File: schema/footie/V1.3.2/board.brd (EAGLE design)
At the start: 53 x 50.6 mm, 41 parts, among them T1 2N3565, U1 IRLML2246TRPBF, U2 USD-SOCKETNEW, U4 MCP73831, U5 3.3 regulator, U6 ATMEGA328P-AU

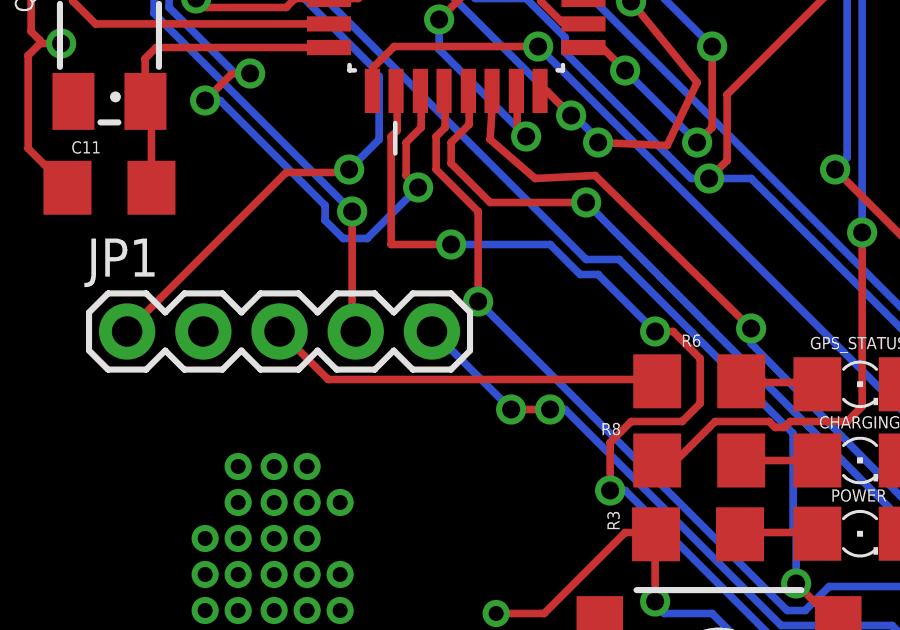
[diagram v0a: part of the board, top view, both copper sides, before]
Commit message: update parser fix schematic wiring
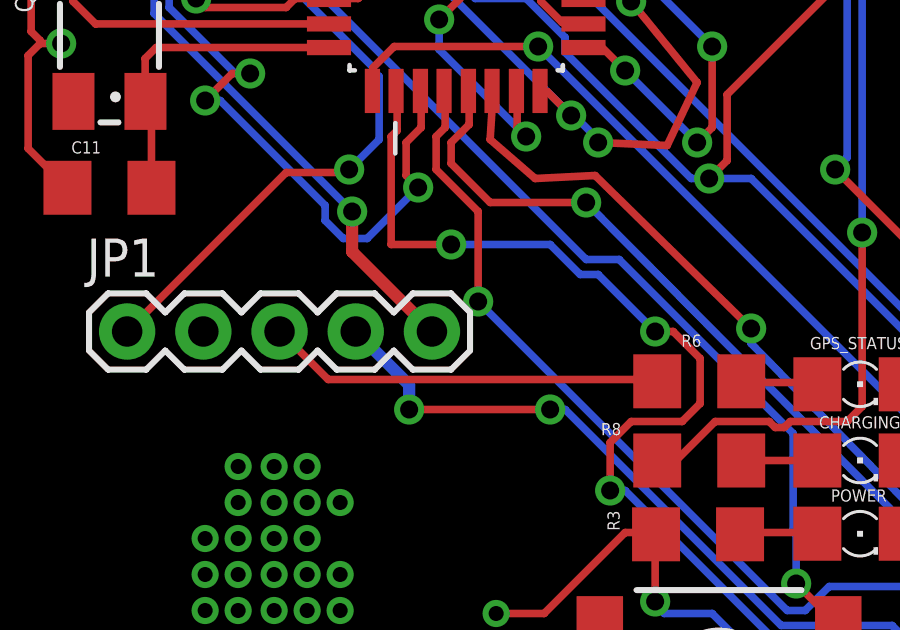
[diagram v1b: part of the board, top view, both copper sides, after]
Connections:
- net ARDUINO_RX: now also JP1.5; no longer JP1.4
- net ARDUINO_TX: now also JP1.4; no longer JP1.5
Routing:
- net ARDUINO_TX: track 104.3 -> 107.3 mm
- net ARDUINO_RX: track 77.5 -> 78.7 mm
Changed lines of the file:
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@@
 <contactref element="U6" pad="31"/>
 <contactref element="DEBUG" pad="5"/>
-<contactref element="JP1" pad="5"/>
 <wire x1="39.7" y1="44.6" x2="37.8" y2="42.7" width="0.254" layer="1"/>
 <wire x1="39.9" y1="44.6" x2="39.7" y2="44.6" width="0.254" layer="1"/>
@@
 <via x="23.8" y="21.9" extent="1-16" drill="0.6"/>
 <via x="13.8" y="31.4" extent="1-16" drill="0.6"/>
-<wire x1="14.6" y1="16.8" x2="17.2" y2="14.2" width="0.254" layer="16"/>
-<wire x1="14.6" y1="16.8" x2="14.56" y2="16.8" width="0.254" layer="16"/>
-<wire x1="18.5" y1="14.2" x2="17.2" y2="14.2" width="0.254" layer="1"/>
+<wire x1="18.5" y1="14.2" x2="13.8" y2="14.2" width="0.254" layer="1"/>
 <wire x1="19" y1="14.2" x2="18.5" y2="14.2" width="0.254" layer="16"/>
 <wire x1="26.2" y1="7" x2="19" y2="14.2" width="0.254" layer="16"/>
@@
 <wire x1="25.2" y1="21.9" x2="35.9" y2="11.2" width="0.254" layer="16"/>
 <wire x1="23.8" y1="21.9" x2="25.2" y2="21.9" width="0.254" layer="16"/>
-<via x="17.2" y="14.2" extent="1-16" drill="0.6"/>
+<via x="13.8" y="14.2" extent="1-16" drill="0.6"/>
 <via x="18.5" y="14.2" extent="1-16" drill="0.6"/>
 <via x="39.8" y="4.4" extent="1-16" drill="0.6"/>
 <via x="37.5" y="9.2" extent="1-16" drill="0.6"/>
+<contactref element="JP1" pad="4"/>
+<wire x1="13.8" y1="14.2" x2="13.8" y2="15.02" width="0.4064" layer="16"/>
+<wire x1="13.8" y1="15.02" x2="12.02" y2="16.8" width="0.4064" layer="16"/>
 </signal>
 <signal name="ARDUINO_RX">
 <contactref element="U6" pad="30"/>
 <contactref element="DEBUG" pad="6"/>
-<contactref element="JP1" pad="4"/>
 <wire x1="37.4" y1="46.4" x2="36" y2="47.8" width="0.254" layer="1"/>
 <wire x1="39.5" y1="46.4" x2="37.4" y2="46.4" width="0.254" layer="1"/>
@@
 <via x="9.5" y="35" extent="1-16" drill="0.6"/>
 <via x="11.7" y="34.8" extent="1-16" drill="0.6"/>
-<wire x1="11.9" y1="16.9" x2="11.9" y2="20.8" width="0.254" layer="1"/>
-<wire x1="12" y1="16.8" x2="11.9" y2="16.9" width="0.254" layer="1"/>
-<wire x1="12" y1="16.8" x2="12.02" y2="16.8" width="0.254" layer="1"/>
+<wire x1="14.6" y1="16.8" x2="14.5" y2="16.9" width="0.254" layer="1"/>
 <wire x1="5.3" y1="27.4" x2="11.9" y2="20.8" width="0.254" layer="16"/>
 <wire x1="5.3" y1="28.8" x2="5.3" y2="27.4" width="0.254" layer="16"/>
@@
 <wire x1="7.1" y1="34.9" x2="7.1" y2="30.6" width="0.254" layer="16"/>
 <via x="11.9" y="20.8" extent="1-16" drill="0.6"/>
+<contactref element="JP1" pad="5"/>
+<wire x1="11.9" y1="20.8" x2="11.9" y2="19.46" width="0.4064" layer="1"/>
+<wire x1="11.9" y1="19.46" x2="14.56" y2="16.8" width="0.4064" layer="1"/>
+<wire x1="14.56" y1="16.8" x2="14.6" y2="16.8" width="0" layer="19" extent="1-1"/>
 </signal>
 <signal name="DTR">
